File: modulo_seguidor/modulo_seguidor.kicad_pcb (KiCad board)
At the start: 2 copper layers, 146.3 x 79.8 mm, 29 parts, among them J1 Battery, J2 Motor A Entradas, J4 Motor IZQ Arduino OUTPUT, J6 puerto sensores, M1 Motor_IZQ, M2 Motor_DER, SW1 SW_Push, SW2 SW_Nidec_CAS-120A1, U1 LM7806_TO220, U2 L298N

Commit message: Cambios placa sensor
Se asignaron pines distintos para los motores, se movieron  varias cosas y está el intento de sumar el modulo hm-10
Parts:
- removed J2: Motor A Entradas, Connector_Molex:Molex_KK-254_AE-6410-02A_1x02_P2.54mm_Vertical
- removed J4: Motor IZQ Arduino OUTPUT, Connector_Molex:Molex_KK-254_AE-6410-02A_1x02_P2.54mm_Vertical
- removed R1: 1k, Resistor_SMD:R_1206_3216Metric_Pad1.30x1.75mm_HandSolder
- added H1: MountingHole, MountingHole:MountingHole_3.2mm_M3, F.Cu at (78.7, 126.4)
- added H1: MountingHole, MountingHole:MountingHole_3.2mm_M3, F.Cu at (78.7, 65.0)
- added H10: MountingHole, MountingHole:MountingHole_3.2mm_M3, F.Cu at (93.3, 75.0)
- added H11: MountingHole, MountingHole:MountingHole_3.2mm_M3, F.Cu at (3.48, 27.3)
- added H11: MountingHole, MountingHole:MountingHole_3.2mm_M3, F.Cu at (93.3, 136.5)
- added H12: MountingHole, MountingHole:MountingHole_3.2mm_M3, F.Cu at (131.1, 64.6)
- added H2: MountingHole, MountingHole:MountingHole_3.2mm_M3, F.Cu at (3.48, 3.48)
- added H3: MountingHole, MountingHole:MountingHole_3.2mm_M3, F.Cu at (78.2, 95.1)
- added H4: MountingHole, MountingHole:MountingHole_3.2mm_M3, F.Cu at (93.3, 65.0)
- added H5: MountingHole, MountingHole:MountingHole_3.2mm_M3, F.Cu at (3.48, 11.4)
- added H5: MountingHole, MountingHole:MountingHole_3.2mm_M3, F.Cu at (93.3, 126.4)
- added H6: MountingHole, MountingHole:MountingHole_3.2mm_M3, F.Cu at (78.2, 109.3)
- added H7: MountingHole, MountingHole:MountingHole_3.2mm_M3, F.Cu at (78.7, 136.5)
- added H7: MountingHole, MountingHole:MountingHole_3.2mm_M3, F.Cu at (78.7, 75.0)
- added H8: MountingHole, MountingHole:MountingHole_3.2mm_M3, F.Cu at (3.48, 19.4)
- added H9: MountingHole, MountingHole:MountingHole_3.2mm_M3, F.Cu at (131.1, 137.3)
- J6: footprint Connector_PinHeader_2.54mm:PinHeader_1x08_P2.54mm_Horizontal -> Connector_PinSocket_2.54mm:PinSocket_1x08_P2.54mm_Horizontal
- moved R2 54.4 mm to (113.5, 134.9), turned to 180 degrees
- moved SW1 50.5 mm to (117.2, 79.2), turned to 180 degrees
- moved D1 44.5 mm to (120.4, 134.8), turned to 0 degrees
- moved G*** 39.4 mm to (56.3, 153.7)
- moved C4 26.9 mm to (126.4, 97.8), turned to 90 degrees
- moved J1 19.3 mm to (88.0, 97.2), turned to 0 degrees
- moved D5 13.9 mm to (107.4, 117.0)
- moved C2 13.8 mm to (108.2, 104.2), turned to -90 degrees
- moved D8 12.5 mm to (100.6, 124.6)
- moved D7 12.3 mm to (100.6, 79.1)
- moved D6 11.7 mm to (121.0, 116.8)
- moved D2 11.5 mm to (121.0, 86.9)
- moved D9 11.1 mm to (126.0, 124.5)
- moved D3 10.2 mm to (107.4, 86.8)
- moved D4 8.85 mm to (126.0, 79.2)
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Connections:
- A1 pad 10: unconnected-(A1-D7-Pad10) -> /Motor DER Arduino DIG OUTPUT
- A1 pad 11: unconnected-(A1-D8-Pad11) -> /Motor DER Arduino PWM OUTPUT
- A1 pad 12: /Motor DER Arduino DIG OUTPUT -> unconnected-(A1-D9-Pad12)
- A1 pad 13: /Motor DER Arduino PWM OUTPUT -> unconnected-(A1-D10-Pad13)
- A1 pad 15: /Boton_encendido -> Net-(A1-D12)
- A1 pad 20: Net-(A1-A1) -> unconnected-(A1-A1-Pad20)
- A1 pad 5: Net-(A1-D2) -> /Motor IZQ Arduino DIG OUTPUT
- A1 pad 6: Net-(A1-D3) -> /Motor IZQ Arduino PWM OUTPUT
- A1 pad 7: unconnected-(A1-D4-Pad7) -> /Boton_encendido
- D1 pad 2: Net-(A1-A1) -> Net-(A1-D12)
- SW1 pad 1: +5V -> GND
- U2 pad 5: Net-(J2-Pin_2) -> /Motor IZQ Arduino DIG OUTPUT
- U2 pad 7: Net-(J2-Pin_1) -> /Motor IZQ Arduino PWM OUTPUT
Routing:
- net /Motor IZQ Arduino PWM OUTPUT: track 0.00 -> 95.7 mm, vias 0 -> 2
- net /Motor IZQ Arduino DIG OUTPUT: track 0.00 -> 75.9 mm, vias 0 -> 2
- net /Boton_encendido: track 15.2 -> 52.7 mm
- net +5V: track 136.6 -> 113.5 mm
- net Net-(A1-D12): track 0.00 -> 22.9 mm
- net GND: track 39.4 -> 18.5 mm, vias 2 -> 0
- net Salida Regulador: track 18.0 -> 28.1 mm
- net Net-(J2-Pin_2): track 7.62 -> 0.00 mm
- net Net-(J2-Pin_1): track 7.62 -> 0.00 mm
- net Net-(A1-D3): track 5.64 -> 0.00 mm
- net Net-(A1-D2): track 5.64 -> 0.00 mm
- net Net-(D3-K): track 28.1 -> 22.8 mm
- net Net-(A1-A1): track 4.97 -> 0.00 mm
- net /Sensor5: track 66.2 -> 62.5 mm
- net /Sensor6: track 66.2 -> 62.9 mm
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- removed copper zone on B.Cu, net Salida Regulador
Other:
- board size 146.3 x 79.8 mm -> 146.3 x 80 mm

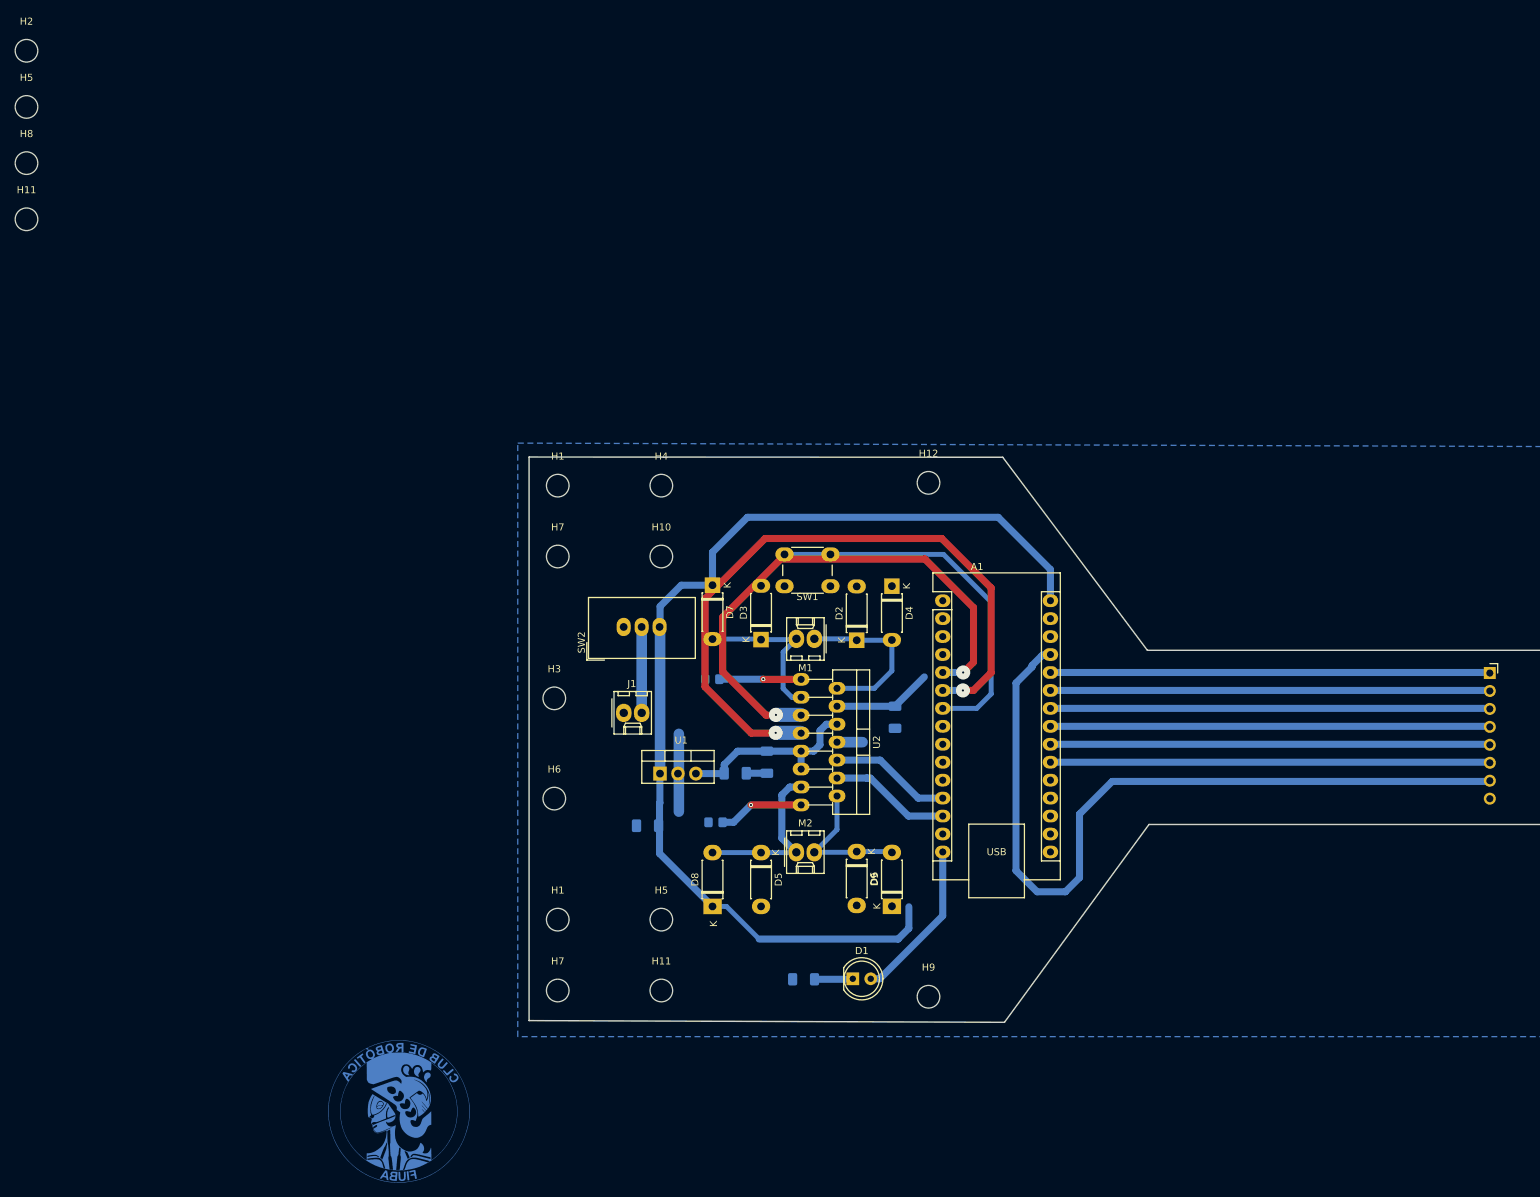
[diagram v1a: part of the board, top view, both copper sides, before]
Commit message: Actualizaciones de la ultima placa del seguidor
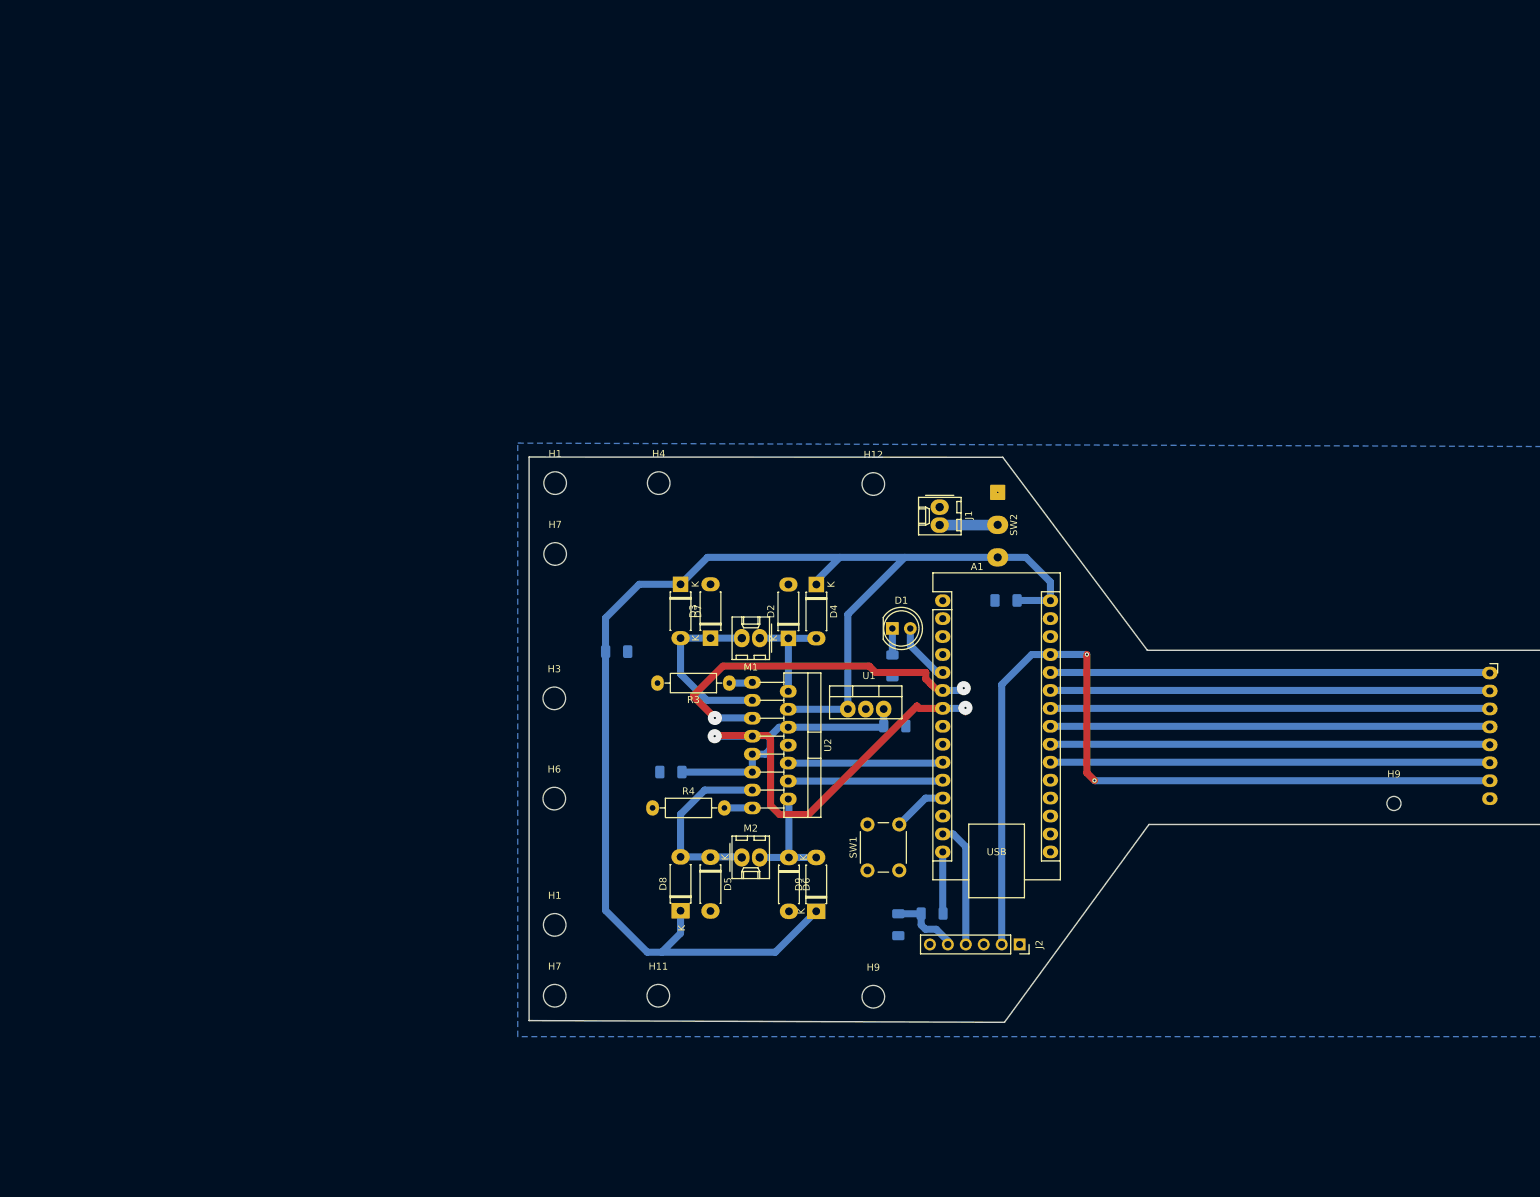
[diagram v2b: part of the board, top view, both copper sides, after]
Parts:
- removed G***: LOGO, FIUBA_Media:CDR_Logo_20x20.1_Inverted
- removed H10, H2, H5 (x2), H8: MountingHole, MountingHole:MountingHole_3.2mm_M3
- removed the H11 at (3.48, 27.3)
- added H9: MountingHole, MountingHole:MountingHole_3.2mm_M3, F.Cu at (197.0, 110.0)
- added J2: Modulo_HM10, Connector_PinSocket_2.54mm:PinSocket_1x06_P2.54mm_Vertical, F.Cu at (144.0, 129.9)
- added R5: 1k, Resistor_SMD:R_1206_3216Metric_Pad1.30x1.75mm_HandSolder, B.Cu at (131.6, 125.6)
- added R6: 2k, Resistor_SMD:R_1206_3216Metric_Pad1.30x1.75mm_HandSolder, B.Cu at (126.9, 127.2)
- R3, R4: footprint Resistor_SMD:R_0805_2012Metric_Pad1.20x1.40mm_HandSolder -> Resistor_THT:R_Axial_DIN0207_L6.3mm_D2.5mm_P10.16mm_Horizontal; moved to F.Cu
- SW1: footprint Button_Switch_THT:SW_PUSH_6mm -> Button_Switch_THT:SW_PUSH_6mm_H5mm
- SW2: footprint Converter_DCDC:Converter_DCDC_TRACO_TSR2-xxxx_THT -> Connector_Wire:SolderWire-0.5sqmm_1x03_P4.6mm_D0.9mm_OD2.1mm
- moved C1 59.9 mm to (142.1, 81.3)
- moved SW2 56.3 mm to (140.9, 66.0), turned to -90 degrees
- moved J1 53.4 mm to (132.7, 68.1), turned to -90 degrees
- moved D1 49.9 mm to (126.0, 85.2)
- moved R2 46.1 mm to (126.0, 90.5), turned to -90 degrees
- moved SW1 40.6 mm to (122.5, 119.5), turned to 90 degrees
- moved C4 40.5 mm to (87.0, 88.5), turned to 180 degrees
- moved U1 28.1 mm to (119.7, 96.6)
- moved C2 18.8 mm to (126.4, 99.0), turned to 0 degrees
- moved D9 10.7 mm to (115.2, 125.3)
- moved D4 10.7 mm to (115.3, 79.0)
- moved D2 9.67 mm to (111.3, 86.6)
- moved D6 9.63 mm to (111.4, 117.6)
- moved R4 9.14 mm to (92.1, 110.6)
- moved C3 9.11 mm to (94.7, 105.5), turned to 0 degrees
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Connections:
- A1 pad 12: unconnected-(A1-D9-Pad12) -> /Boton_encendido
- A1 pad 14: unconnected-(A1-D11-Pad14) -> /TX
- A1 pad 15: Net-(A1-D12) -> /RX
- A1 pad 5: /Motor IZQ Arduino DIG OUTPUT -> Net-(A1-D2)
- A1 pad 6: /Motor IZQ Arduino PWM OUTPUT -> /Motor IZQ Arduino DIG OUTPUT
- A1 pad 7: /Boton_encendido -> /Motor IZQ Arduino PWM OUTPUT
- D1 pad 2: Net-(A1-D12) -> Net-(A1-D2)
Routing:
- net /Boton_encendido: track 52.7 -> 7.70 mm
- net /Motor IZQ Arduino PWM OUTPUT: track 95.7 -> 58.1 mm
- net VCC: track 164.2 -> 196.9 mm
- net /Motor IZQ Arduino DIG OUTPUT: track 75.9 -> 51.7 mm
- net Net-(A1-D12): track 22.9 -> 0.00 mm
- net GND: track 18.5 -> 0.00 mm
- net /TX: track 0.00 -> 17.8 mm
- net +5V: track 113.5 -> 124.8 mm, vias 0 -> 2
- net Net-(J2-Pin_5): track 0.00 -> 10.1 mm
- net /RX: track 0.00 -> 8.74 mm
- net Net-(D2-K): track 24.2 -> 15.5 mm
- net Net-(A1-D2): track 0.00 -> 8.59 mm
- net Net-(U2-SENSE_A): track 11.7 -> 3.30 mm, vias 1 -> 0
- net Salida Regulador: track 28.1 -> 36.3 mm
- net Net-(U2-SENSE_B): track 11.9 -> 3.96 mm, vias 1 -> 0
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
